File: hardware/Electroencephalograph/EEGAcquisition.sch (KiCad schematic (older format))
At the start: 60 parts, among them U1 ADS1298IPAG, U2 OPA330xxD

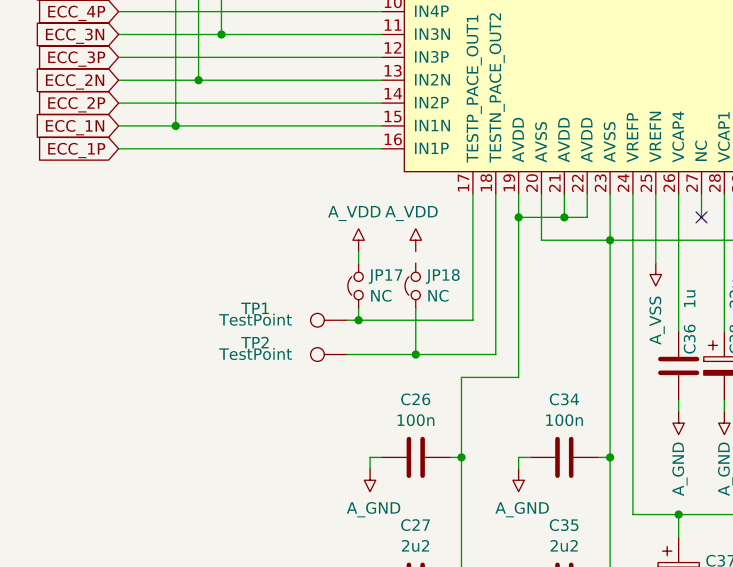
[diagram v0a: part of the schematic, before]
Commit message: fixed spi lines
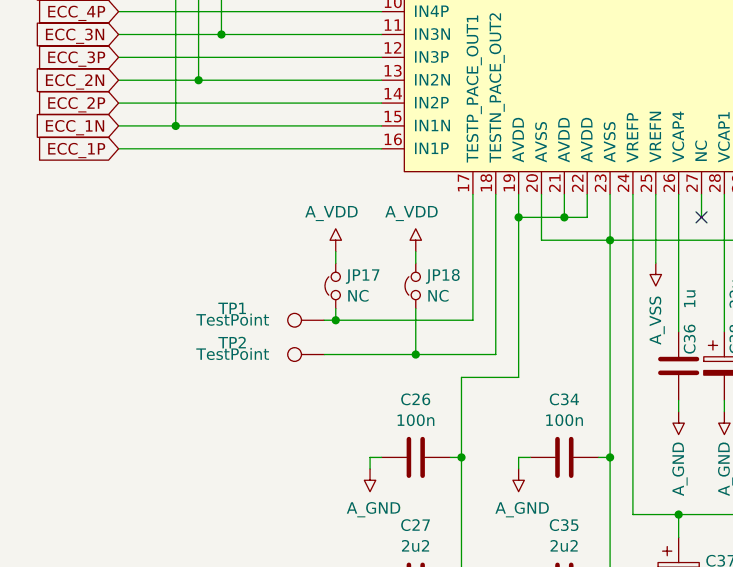
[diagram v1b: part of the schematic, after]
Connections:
- net A_VDD: now also JP18.1
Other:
- moved on the sheet: JP17, TP1, TP2
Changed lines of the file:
@@
 	2600 5300 2600 5850
 Wire Wire Line
-	2600 5850 2100 5850
+	2600 5850 2000 5850
 Wire Wire Line
 	2700 5300 2700 6000
@@
 L Connector:TestPoint TP1
 U 1 1 5E170075
-P 2050 5850
-F 0 "TP1" V 2100 6250 50  0000 C CNN
-F 1 "TestPoint" V 2050 6250 50  0000 C CNN
-F 2 "TestPoint:TestPoint_Pad_1.5x1.5mm" H 2250 5850 50  0001 C CNN
-F 3 "~" H 2250 5850 50  0001 C CNN
-	1    2050 5850
+P 1950 5850
+F 0 "TP1" V 2000 6250 50  0000 C CNN
+F 1 "TestPoint" V 1950 6250 50  0000 C CNN
+F 2 "TestPoint:TestPoint_Pad_1.5x1.5mm" H 2150 5850 50  0001 C CNN
+F 3 "~" H 2150 5850 50  0001 C CNN
+	1    1950 5850
 	0    -1   -1   0
 $EndComp
@@
 L Connector:TestPoint TP2
 U 1 1 5E19AC83
-P 2050 6000
-F 0 "TP2" V 2100 6400 50  0000 C CNN
-F 1 "TestPoint" V 2050 6400 50  0000 C CNN
-F 2 "TestPoint:TestPoint_Pad_1.5x1.5mm" H 2250 6000 50  0001 C CNN
-F 3 "~" H 2250 6000 50  0001 C CNN
-	1    2050 6000
+P 1950 6000
+F 0 "TP2" V 2000 6400 50  0000 C CNN
+F 1 "TestPoint" V 1950 6400 50  0000 C CNN
+F 2 "TestPoint:TestPoint_Pad_1.5x1.5mm" H 2150 6000 50  0001 C CNN
+F 3 "~" H 2150 6000 50  0001 C CNN
+	1    1950 6000
 	0    -1   -1   0
 $EndComp
@@
 L Electroencephalograph:A_VDD #PWR50
 U 1 1 5E36352C
-P 2100 5550
-F 0 "#PWR50" H 2100 5650 50  0001 C CNN
-F 1 "A_VDD" H 2117 5723 50  0000 C CNN
-F 2 "" H 2100 5650 50  0001 C CNN
-F 3 "" H 2100 5650 50  0001 C CNN
-	1    2100 5550
+P 2000 5550
+F 0 "#PWR50" H 2000 5650 50  0001 C CNN
+F 1 "A_VDD" H 2017 5723 50  0000 C CNN
+F 2 "" H 2000 5650 50  0001 C CNN
+F 3 "" H 2000 5650 50  0001 C CNN
+	1    2000 5550
 	-1   0    0    -1
 $EndComp
@@
 L Device:Jumper_NC_Small JP?
 U 1 1 5E36438E
-P 2100 5700
+P 2000 5700
 AR Path="/5DFE0AD6/5E36438E" Ref="JP?"  Part="1"
 AR Path="/5DF61103/5E36438E" Ref="JP17"  Part="1"
-F 0 "JP17" V 2054 5652 50  0000 R CNN
-F 1 "NC" V 2145 5652 50  0000 R CNN
-F 2 "Jumper:SolderJumper-2_P1.3mm_Bridged_Pad1.0x1.5mm" H 2100 5700 50  0001 C CNN
-F 3 "~" H 2100 5700 50  0001 C CNN
-	1    2100 5700
+F 0 "JP17" V 1954 5652 50  0000 R CNN
+F 1 "NC" V 2045 5652 50  0000 R CNN
+F 2 "Jumper:SolderJumper-2_P1.3mm_Bridged_Pad1.0x1.5mm" H 2000 5700 50  0001 C CNN
+F 3 "~" H 2000 5700 50  0001 C CNN
+	1    2000 5700
 	0    -1   1    0
 $EndComp
@@
 $EndComp
 Wire Wire Line
-	2100 5550 2100 5600
-Wire Wire Line
-	2100 5800 2100 5850
-Connection ~ 2100 5850
-Wire Wire Line
-	2100 5850 2050 5850
+	2000 5550 2000 5600
+Wire Wire Line
+	2000 5800 2000 5850
+Connection ~ 2000 5850
+Wire Wire Line
+	2000 5850 1950 5850
 Wire Wire Line
 	2350 5800 2350 6000
 Connection ~ 2350 6000
 Wire Wire Line
-	2350 6000 2050 6000
+	2350 6000 1950 6000
 Wire Wire Line
 	2900 3350 2900 3200
@@
 Text Label 10450 5400 0    50   ~ 0
 OPAMP_MAYBE
+Wire Wire Line
+	2350 5600 2350 5550
 $EndSCHEMATC

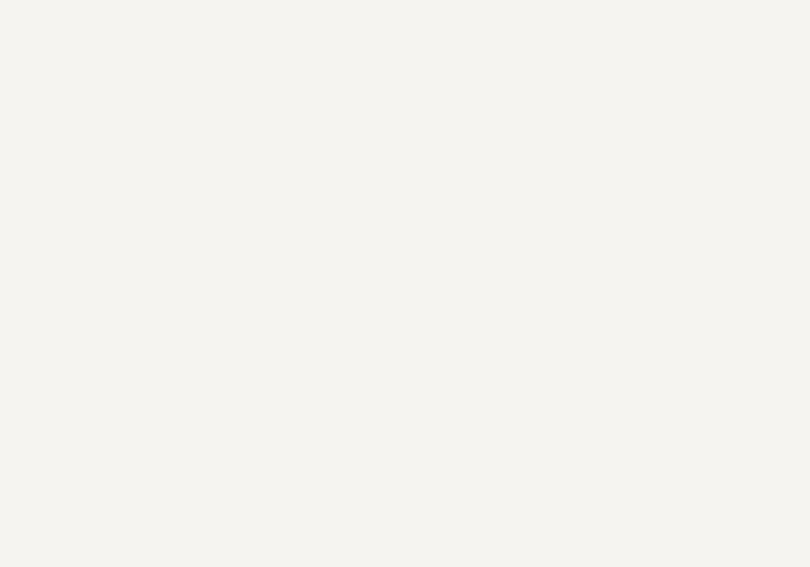
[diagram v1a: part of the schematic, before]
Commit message: added procesing unit
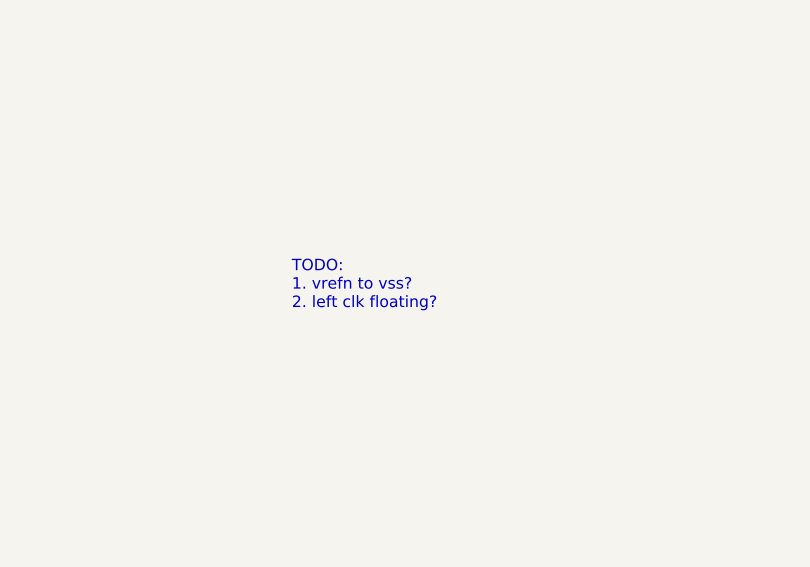
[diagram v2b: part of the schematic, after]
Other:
- note added: "TODO: \n1. vrefn to vss?\n2. left clk floating?"
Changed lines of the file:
@@
 Wire Wire Line
 	2350 5600 2350 5550
+Text Notes 8550 2750 0    50   ~ 0
+TODO: \n1. vrefn to vss?\n2. left clk floating?
 $EndSCHEMATC

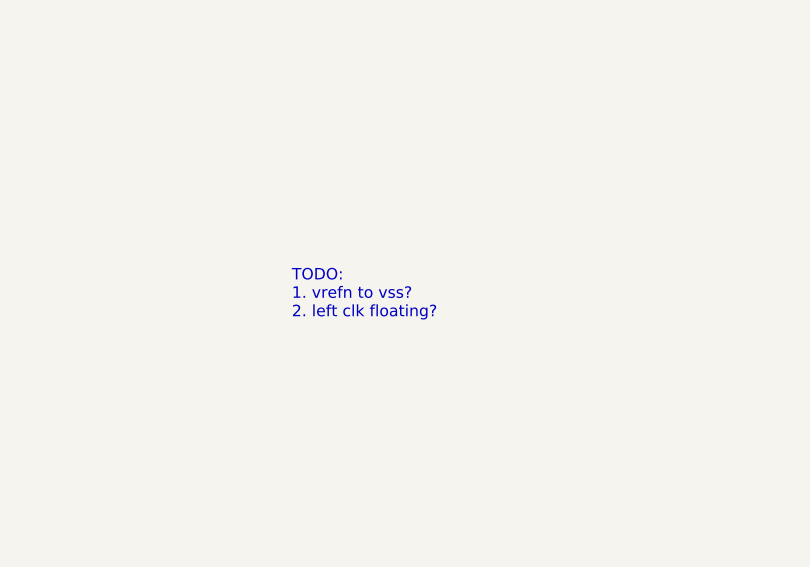
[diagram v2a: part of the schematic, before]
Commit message: eeg digital part routing
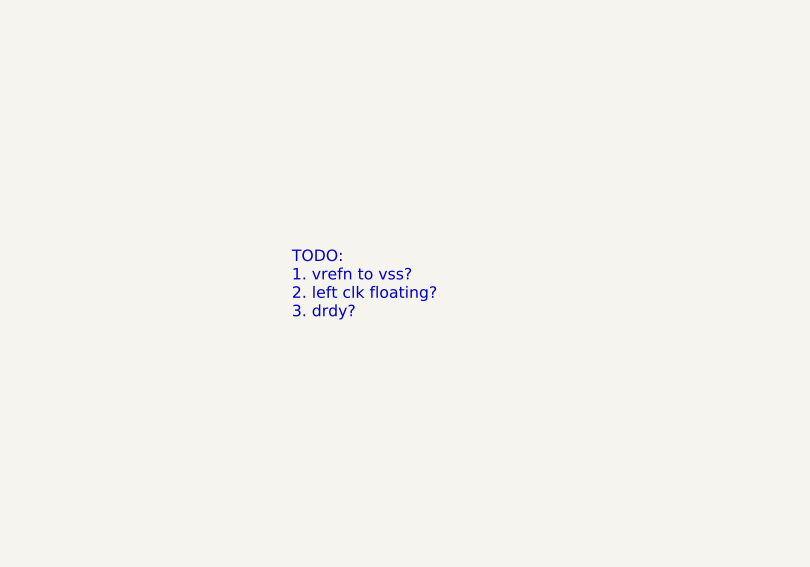
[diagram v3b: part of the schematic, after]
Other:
- note added: "TODO: \n1. vrefn to vss?\n2. left clk floating?\n3. drdy?"
- note removed: "TODO: \n1. vrefn to vss?\n2. left clk floating?"
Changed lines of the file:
@@
 	2350 5600 2350 5550
 Text Notes 8550 2750 0    50   ~ 0
-TODO: \n1. vrefn to vss?\n2. left clk floating?
+TODO: \n1. vrefn to vss?\n2. left clk floating?\n3. drdy?
 $EndSCHEMATC

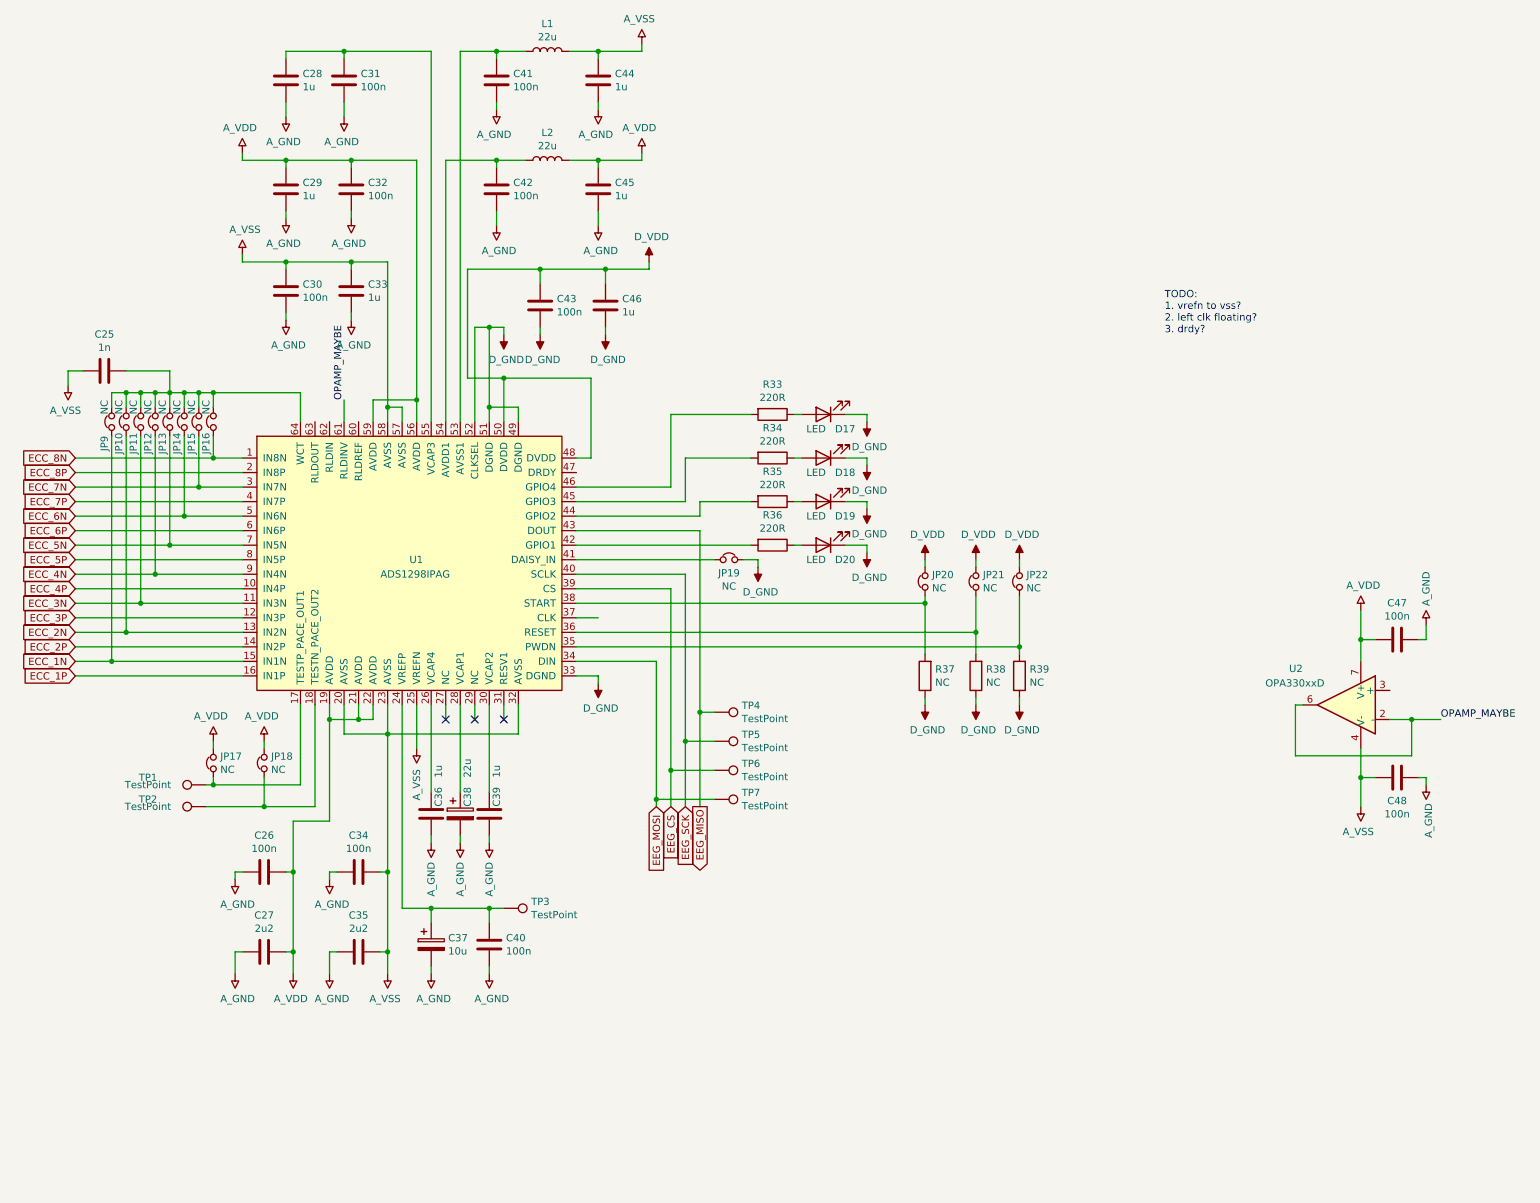
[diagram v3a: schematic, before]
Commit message: routing of analog power supply
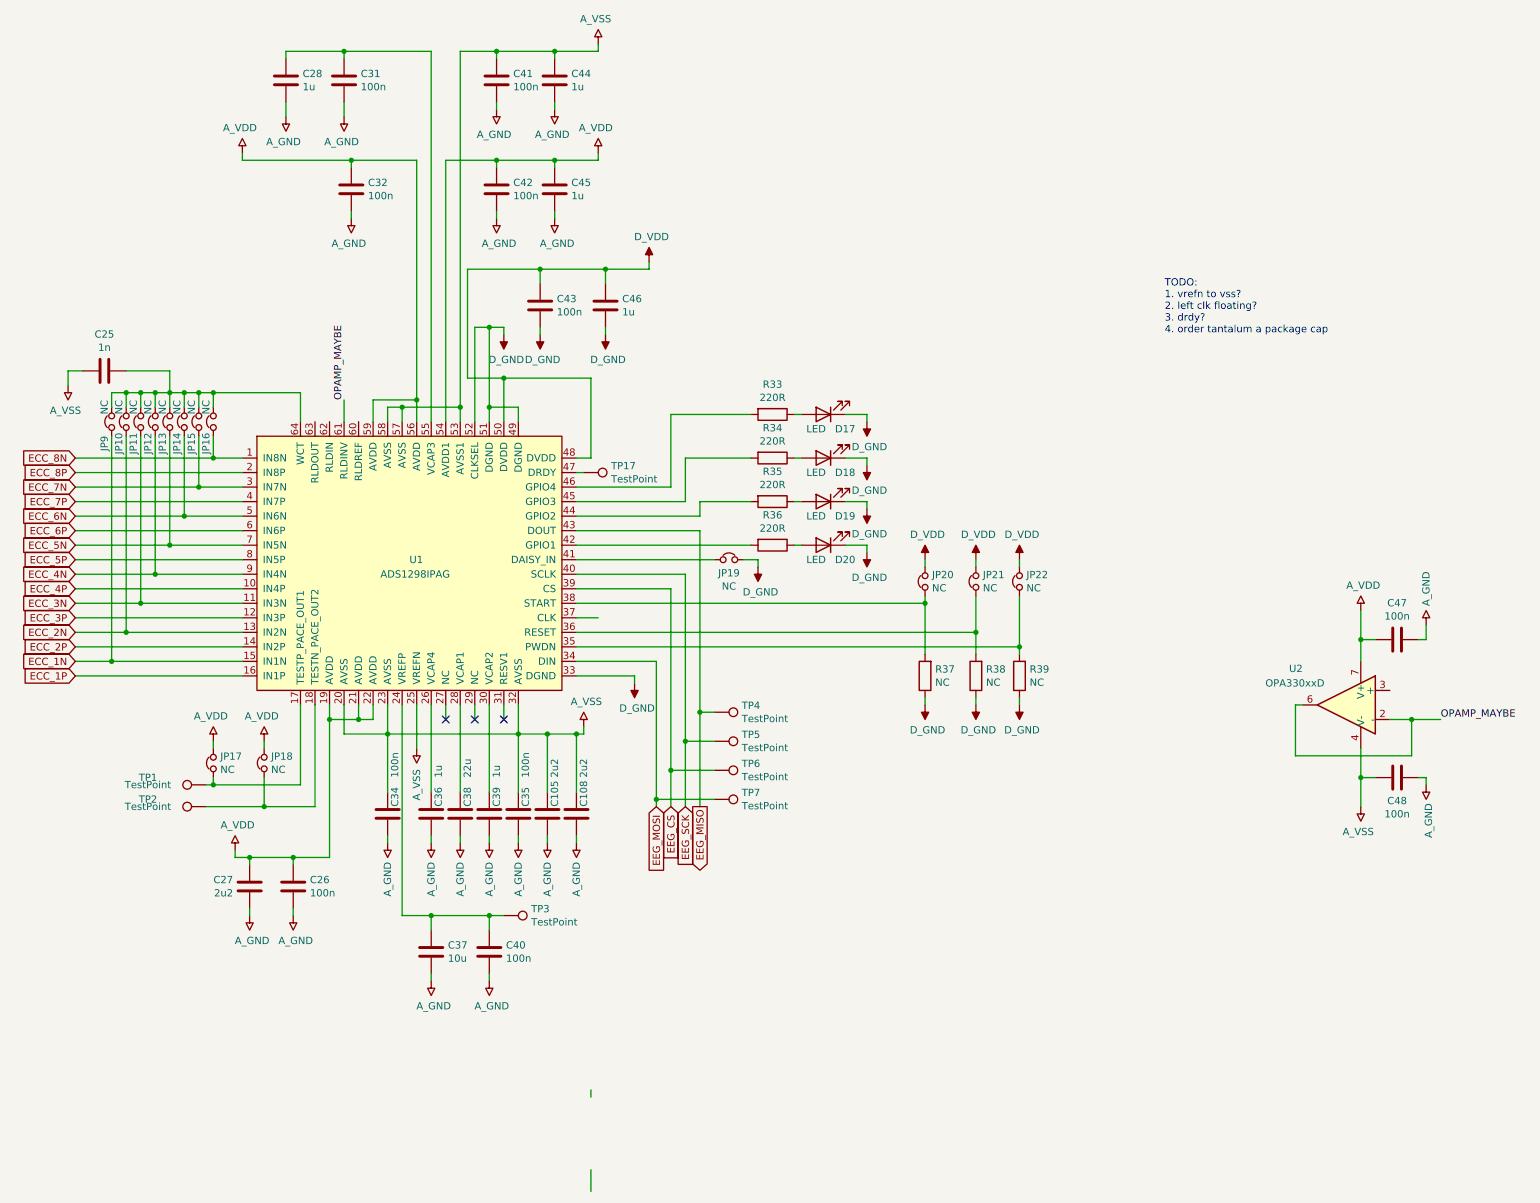
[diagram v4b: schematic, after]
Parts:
- removed C29, C33: 1u, Capacitor_SMD:C_0402_1005Metric, symbol Device:C
- removed C30: 100n, Capacitor_SMD:C_0402_1005Metric, symbol Device:C
- removed C37: 10u, Capacitor_Tantalum_SMD:CP_EIA-3528-21_Kemet-B, symbol Device:CP
- removed C38: 22u, Capacitor_Tantalum_SMD:CP_EIA-3528-21_Kemet-B, symbol Device:CP
- removed L1, L2: 22u, Electroencephalograph:L_7.3x7.3_H3.5, symbol Device:L
- added C105, C108: 2u2, Capacitor_SMD:C_0402_1005Metric, symbol Device:C
- added C37: 10u, Capacitor_SMD:C_0805_2012Metric, symbol Device:C
- added C38: 22u, Capacitor_SMD:C_0805_2012Metric, symbol Device:C
- added TP17: TestPoint, TestPoint:TestPoint_Pad_D1.0mm, symbol Connector:TestPoint
- C35: value 2u2 -> 100n
- TP1, TP2, TP3, TP4, TP5, TP6, TP7: footprint TestPoint:TestPoint_Pad_1.5x1.5mm -> TestPoint:TestPoint_Pad_D1.0mm
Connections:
- net A_GND: now also C26.1, C105.2, C108.2, C37.2, C38.2; no longer C26.2
- net A_VDD: now also C26.2, C42.1, U1.54 (AVDD1); no longer C26.1
- net A_VSS: now also C41.2, U1.53 (AVSS1), C105.1, C108.1
- net at C40.1, TP3.1, U1.24 (VREFP): now also C37.1
- net at U1.28 (VCAP1): now also C38.1
- net at U1.47 (DRDY): now also TP17.1
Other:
- note added: "TODO: \n1. vrefn to vss?\n2. left clk floating?\n3. drdy?\n4. order tantalum a package cap"
- note removed: "TODO: \n1. vrefn to vss?\n2. left clk floating?\n3. drdy?"
- moved on the sheet: C26, C27, C40, C44, C45, TP3

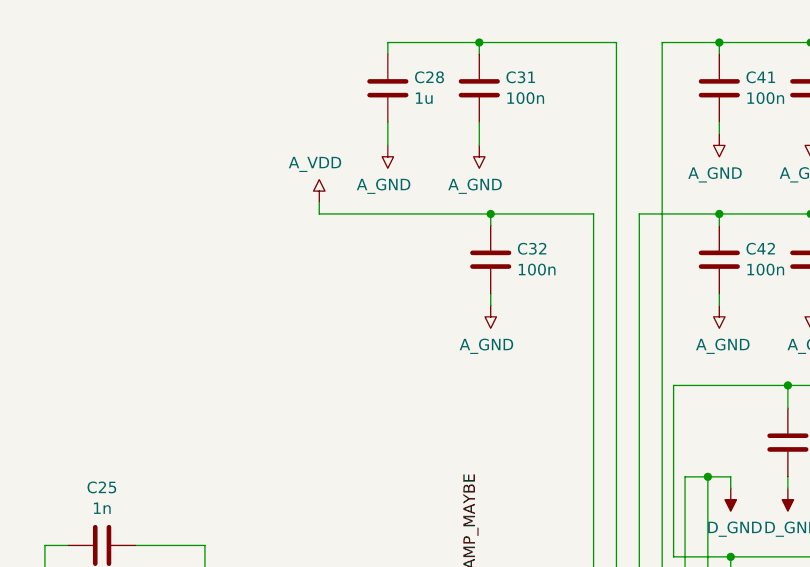
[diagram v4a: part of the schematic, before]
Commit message: route of analog part, update of 3d render
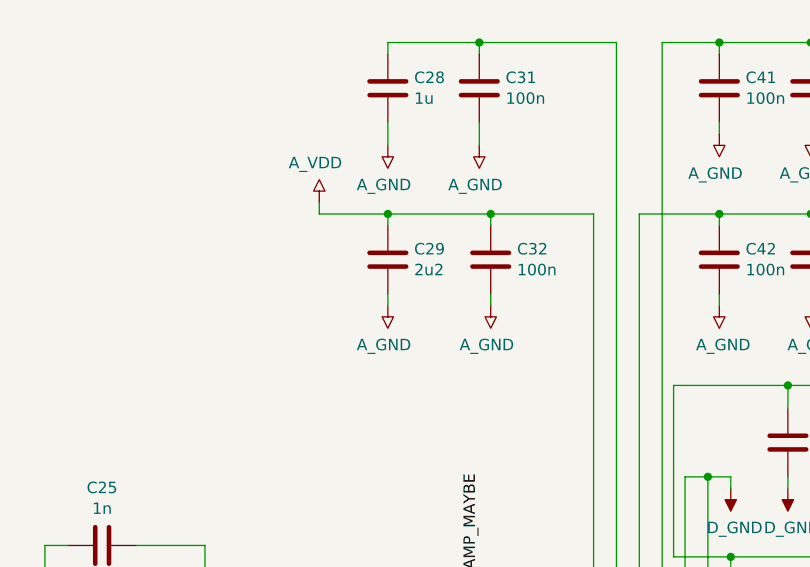
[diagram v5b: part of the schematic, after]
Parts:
- added C29: 2u2, Capacitor_SMD:C_0402_1005Metric, symbol Device:C
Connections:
- net A_GND: now also C29.1
- net A_VDD: now also C29.2
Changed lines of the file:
@@
 $Descr A4 11693 8268
 encoding utf-8
-Sheet 3 7
+Sheet 3 8
 Title ""
 Date ""
@@
 	3700 3250 3700 3350
 Wire Wire Line
-	2200 1550 2950 1550
+	2200 1550 2500 1550
+$Comp
+L Device:C C?
+U 1 1 5E1CE028
+P 2500 1750
+AR Path="/5DF4CFF8/5E1CE028" Ref="C?"  Part="1"
+AR Path="/5DF61103/5E1CE028" Ref="C29"  Part="1"
+F 0 "C29" H 2385 1704 50  0000 R CNN
+F 1 "2u2" H 2385 1795 50  0000 R CNN
+F 2 "Capacitor_SMD:C_0402_1005Metric" H 2538 1600 50  0001 C CNN
+F 3 "~" H 2500 1750 50  0001 C CNN
+	1    2500 1750
+	-1   0    0    1
+$EndComp
+$Comp
+L Electroencephalograph:A_GND #PWR54
+U 1 1 5E1CE02E
+P 2500 1950
+F 0 "#PWR54" H 2500 1975 50  0001 C CNN
+F 1 "A_GND" H 2517 1777 50  0000 C CNN
+F 2 "" H 2500 1975 50  0001 C CNN
+F 3 "" H 2500 1975 50  0001 C CNN
+	1    2500 1950
+	-1   0    0    -1
+$EndComp
+Wire Wire Line
+	2500 1950 2500 1900
+Wire Wire Line
+	2500 1600 2500 1550
+Connection ~ 2500 1550
+Wire Wire Line
+	2500 1550 2950 1550
 $EndSCHEMATC
